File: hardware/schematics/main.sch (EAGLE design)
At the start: 332 parts, among them IC1 74LS257N, IC10 74S181N, IC100 74S257N, IC101 74LS377N, IC102 74LS377N, IC103 74S153N, IC104 74LS257N, IC105 74LS148N, IC106 74LS377N, IC107 74LS74N, IC108 74LS74N, IC109 74LS377N, IC11 74S181N, IC110 74LS377N, IC111 74LS253N, IC112 74LS257N, IC113 74LS253N, IC114 74LS257N, IC115 74LS04N, IC116 74S153N, IC117 74LS377N, IC118 74LS257N, IC119 74S08N, IC12 74LS151N, IC120 74LS244N, IC121 74LS257N, IC122 74LS257N, IC123 74LS377N, IC124 74S153N, IC125 74LS257N, IC126 74LS74N, IC127 74LS257N, IC128 74157N, IC129 74157N, IC13 74LS257N, IC130 74LS151N, IC131 74157N, IC132 74157N, IC133 74LS151N, IC134 74273N, IC135 74273N, IC136 74273N, IC137 74LS74N, IC138 74LS04N, IC139 74LS00N, IC14 74LS151N, IC141 74LS151N, IC142 74LS257N, IC143 74LS08N, IC144 74LS151N, IC145 7410N, IC146 74LS08N, IC147 74LS257N, IC148 74LS00N, IC149 74LS138N, IC15 74LS257N, IC150 74HC244N, IC151 7432N, IC152 74LS151N, IC153 7432N, IC154 74LS04N, IC155 74LS04N, IC156 74LS04N, IC157 74LS377N, IC158 74LS377N, IC159 74LS377N, IC16 74LS151N, IC160 74LS151N, IC161 74LS244N, IC162 74LS377N, IC163 74LS244N, IC164 74LS138N, IC165 74LS377N, IC166 74LS377N, IC167 7432N, IC168 74LS20N, IC169 74LS377N, IC17 74HC244N, IC170 74LS253N, IC171 74LS377N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

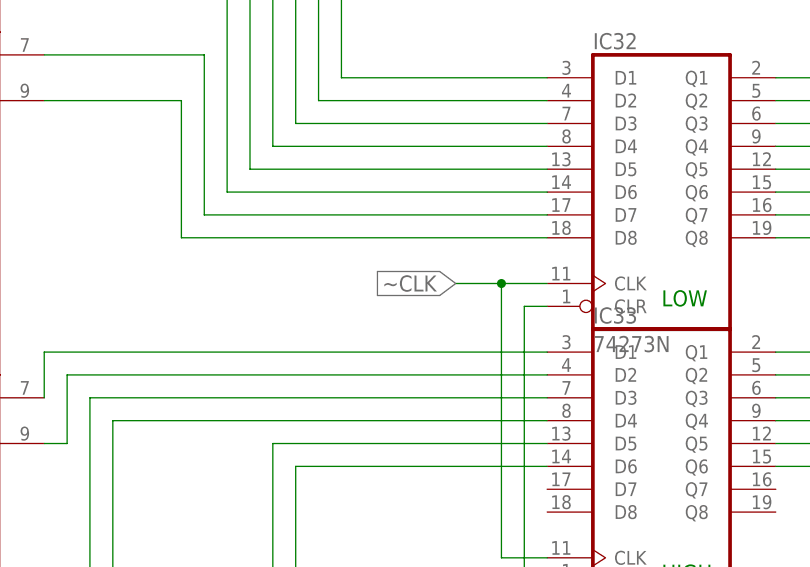
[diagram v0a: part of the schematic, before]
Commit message: initial commit of SystemVerilog RTL for Modelsim.
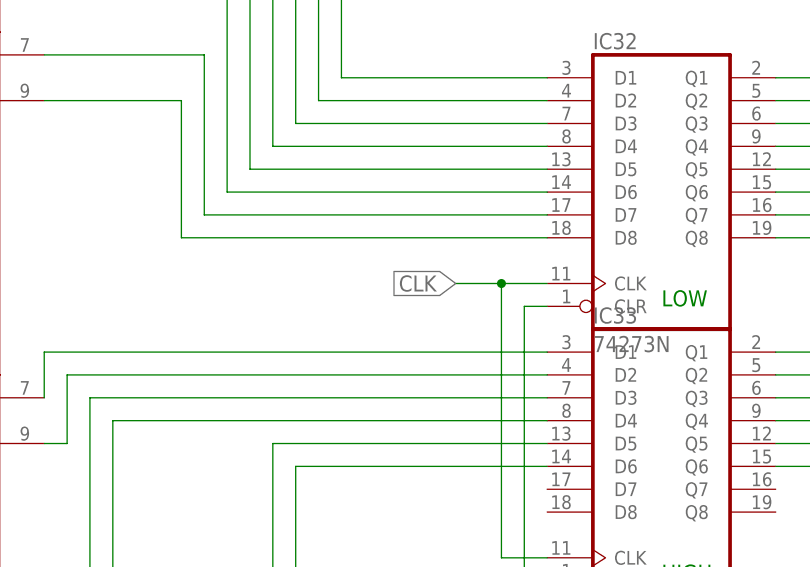
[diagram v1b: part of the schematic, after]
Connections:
- removed net ~CLK: IC32A.CLK, IC33A.CLK
- net CLK: now also IC32A.CLK, IC33A.CLK
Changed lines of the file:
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@@
 <setting verticaltext="up"/>
 </settings>
-<grid distance="0.1" unitdist="inch" unit="inch" style="lines" multiple="1" display="no" altdistance="0.01" altunitdist="inch" altunit="inch"/>
+<grid distance="0.1" unitdist="inch" unit="inch" style="dots" multiple="1" display="yes" altdistance="0.01" altunitdist="inch" altunit="inch"/>
 <layers>
 <layer number="1" name="Top" color="4" fill="1" visible="no" active="no"/>
@@
 <label x="340.36" y="899.16" size="1.778" layer="95" xref="yes"/>
 </segment>
+<segment>
+<pinref part="IC32" gate="A" pin="CLK"/>
+<wire x1="-307.34" y1="586.74" x2="-312.42" y2="586.74" width="0.1524" layer="91"/>
+<wire x1="-312.42" y1="586.74" x2="-312.42" y2="556.26" width="0.1524" layer="91"/>
+<pinref part="IC33" gate="A" pin="CLK"/>
+<wire x1="-312.42" y1="556.26" x2="-307.34" y2="556.26" width="0.1524" layer="91"/>
+<wire x1="-312.42" y1="586.74" x2="-317.5" y2="586.74" width="0.1524" layer="91"/>
+<junction x="-312.42" y="586.74"/>
+<label x="-317.5" y="586.74" size="1.778" layer="95" rot="R180" xref="yes"/>
+</segment>
 </net>
 <net name="YBUS4" class="0">
@@
 </segment>
 </net>
-<net name="~CLK" class="0">
-<segment>
-<pinref part="IC32" gate="A" pin="CLK"/>
-<wire x1="-307.34" y1="586.74" x2="-312.42" y2="586.74" width="0.1524" layer="91"/>
-<wire x1="-312.42" y1="586.74" x2="-312.42" y2="556.26" width="0.1524" layer="91"/>
-<pinref part="IC33" gate="A" pin="CLK"/>
-<wire x1="-312.42" y1="556.26" x2="-307.34" y2="556.26" width="0.1524" layer="91"/>
-<wire x1="-312.42" y1="586.74" x2="-317.5" y2="586.74" width="0.1524" layer="91"/>
-<junction x="-312.42" y="586.74"/>
-<label x="-317.5" y="586.74" size="1.778" layer="95" rot="R180" xref="yes"/>
-</segment>
-</net>
